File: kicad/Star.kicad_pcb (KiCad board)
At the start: 4 copper layers, 104.6 x 99.5 mm, 129 parts, among them J1 10118193-0001LF, J2 Conn_02x03_Odd_Even, SW1 SW_Push, U1 ATmega328P-AU, U2 MCP73831T-2ACI_OT, Y1 8Mhz

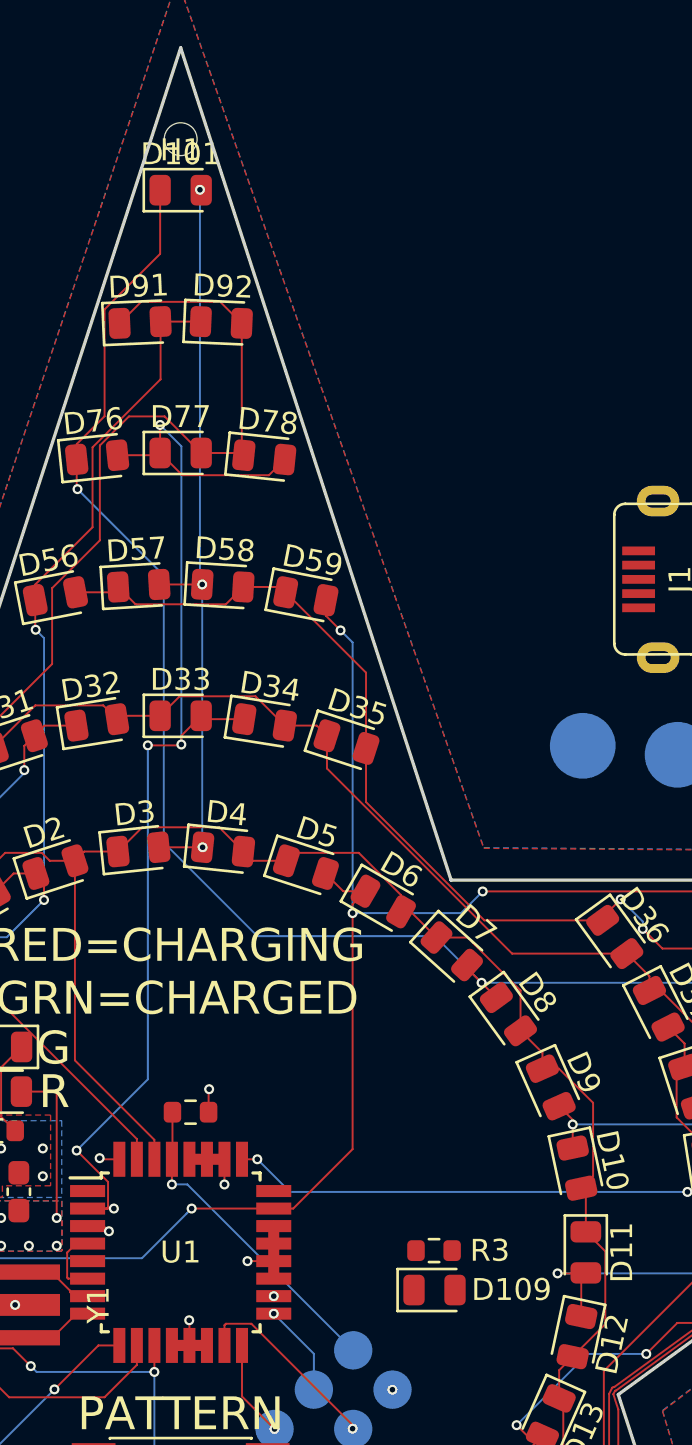
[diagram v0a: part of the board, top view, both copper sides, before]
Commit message: created port settings and display buffers
Port settings are used to turn LEDs on and off.
Buffers are used to display LEDs in a particular pattern.
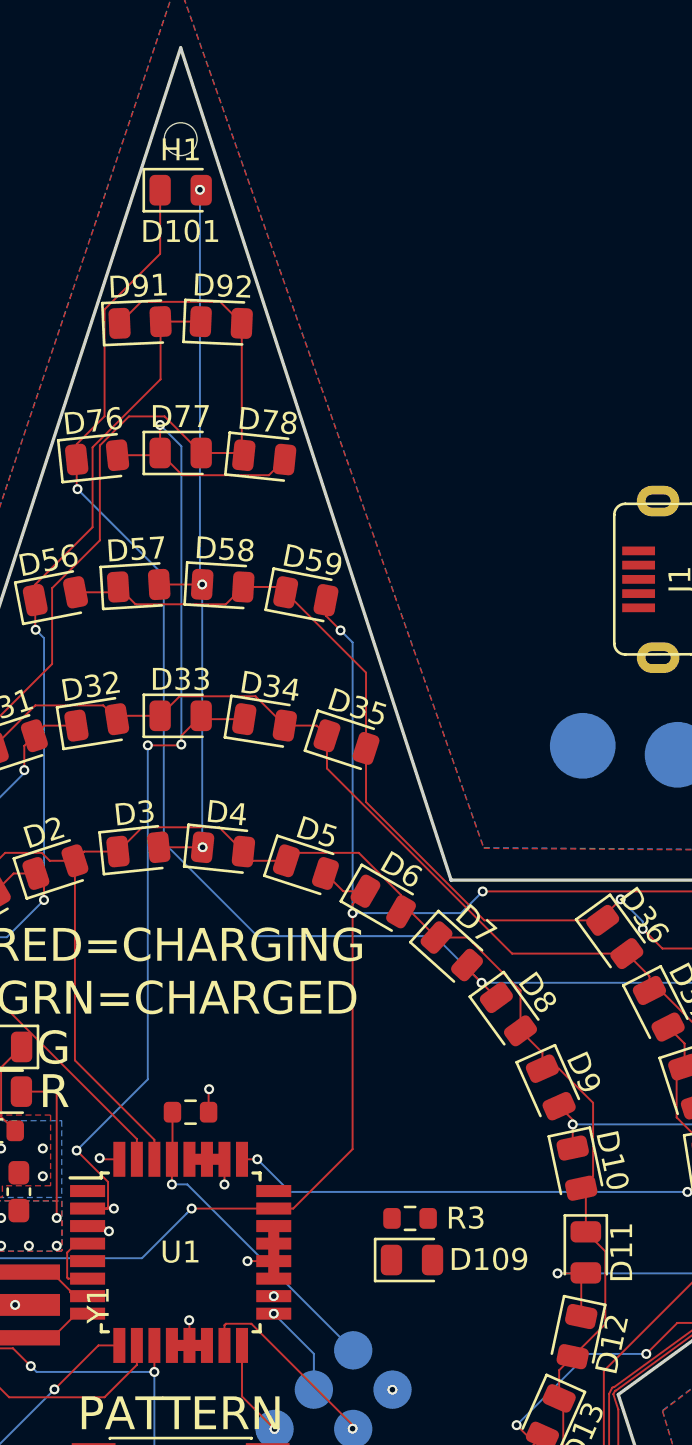
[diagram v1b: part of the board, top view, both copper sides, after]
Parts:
- moved R3 1.83 mm to (110.5, 98.5)
- moved D109 1.71 mm to (110.6, 100.3)

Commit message: jan18 revisions
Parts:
- moved TP5 37.6 mm to (87.8, 108.8)
- moved TP6 36.4 mm to (87.8, 105.5)
- moved J1 25.7 mm to (110.6, 92.4)
- moved TP3 21.8 mm to (121.7, 99.1)
- moved TP4 12.9 mm to (119.0, 89.8)
